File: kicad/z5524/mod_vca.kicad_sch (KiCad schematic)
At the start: 18 parts, among them U12 TL074, U13 AS3364

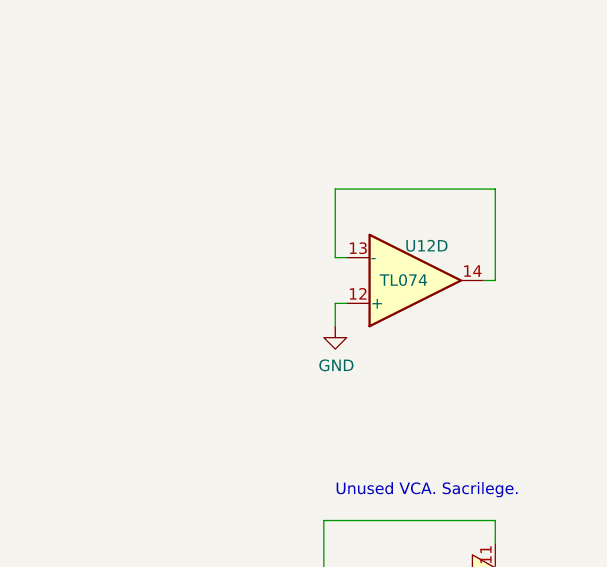
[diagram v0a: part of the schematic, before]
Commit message: move blocks into board for eval
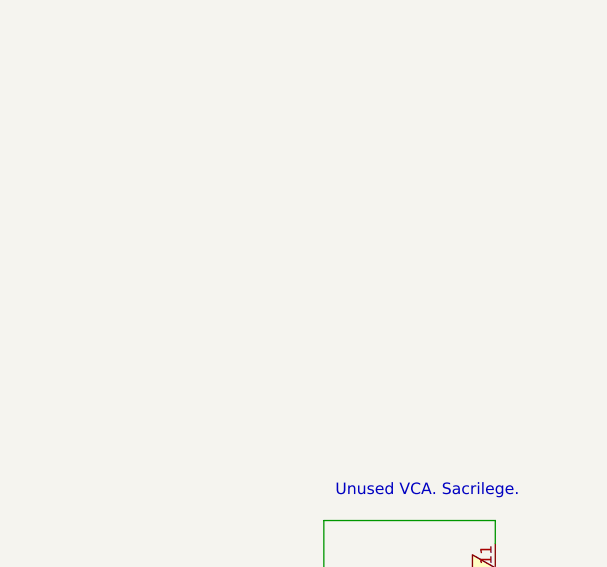
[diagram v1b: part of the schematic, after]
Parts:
- removed unit 4 of U12

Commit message: update to kicad 7
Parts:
- renumbered C39 to C15, C44 to C16, C67 to C18, C66 to C21, C41 to C42, C40 to C46, C42 to C51, C43 to C52, R54 to R19, R86 to R25, R81 to R26, R57 to R27, R85 to R29, R53 to R63, R87 to R64, R55 to R65, U13 to U6, U12 to U8
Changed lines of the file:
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@@
   (symbol (lib_id "Amplifier_Operational:TL074") (at 55.88 240.03 0) (unit 5)
     (in_bom yes) (on_board yes) (fields_autoplaced)
-    (property "Reference" "U12" (id 0) (at 53.975 239.1953 0)
+    (property "Reference" "U8" (id 0) (at 53.975 239.1953 0)
       (effects (font (size 1.27 1.27)) (justify left))
     )
@@
   (symbol (lib_name "AS3364_2") (lib_id "Audio:AS3364") (at 156.21 111.76 0) (unit 3)
     (in_bom yes) (on_board yes) (fields_autoplaced)
-    (property "Reference" "U13" (id 0) (at 160.02 116.84 0))
+    (property "Reference" "U6" (id 0) (at 160.02 116.84 0))
     (property "Value" "AS3364" (id 1) (at 162.56 114.3 0))
     (property "Footprint" "Package_SO:SOIC-16_3.9x9.9mm_P1.27mm" (id 2) (at 158.75 113.03 0)
@@
   (symbol (lib_id "Device:R") (at 180.34 54.61 270) (unit 1)
     (in_bom yes) (on_board yes)
-    (property "Reference" "R55" (id 0) (at 180.34 52.07 90))
+    (property "Reference" "R65" (id 0) (at 180.34 52.07 90))
     (property "Value" "47k" (id 1) (at 180.34 57.15 90))
     (property "Footprint" "Resistor_SMD:R_0603_1608Metric" (id 2) (at 180.34 52.832 90)
@@
   (symbol (lib_id "Amplifier_Operational:TL074") (at 180.34 69.85 0) (mirror x) (unit 3)
     (in_bom yes) (on_board yes)
-    (property "Reference" "U12" (id 0) (at 181.61 64.77 0))
+    (property "Reference" "U8" (id 0) (at 181.61 64.77 0))
     (property "Value" "TL074" (id 1) (at 180.34 69.85 0))
     (property "Footprint" "Package_SO:TSSOP-14_4.4x5mm_P0.65mm" (id 2) (at 179.07 72.39 0)
@@
   (symbol (lib_id "Device:C") (at 180.34 46.99 90) (unit 1)
     (in_bom yes) (on_board yes)
-    (property "Reference" "C43" (id 0) (at 178.435 42.545 0))
+    (property "Reference" "C52" (id 0) (at 178.435 42.545 0))
     (property "Value" "33p" (id 1) (at 182.245 42.545 0))
     (property "Footprint" "Capacitor_SMD:C_0603_1608Metric" (id 2) (at 184.15 46.0248 0)
@@
   (symbol (lib_id "Amplifier_Operational:TL074") (at 180.34 160.02 0) (mirror x) (unit 2)
     (in_bom yes) (on_board yes)
-    (property "Reference" "U12" (id 0) (at 181.61 154.94 0))
+    (property "Reference" "U8" (id 0) (at 181.61 154.94 0))
     (property "Value" "TL074" (id 1) (at 179.07 160.02 0))
     (property "Footprint" "Package_SO:TSSOP-14_4.4x5mm_P0.65mm" (id 2) (at 179.07 162.56 0)
@@
   (symbol (lib_id "Device:R") (at 143.51 67.31 90) (unit 1)
     (in_bom yes) (on_board yes)
-    (property "Reference" "R53" (id 0) (at 143.51 64.77 90))
+    (property "Reference" "R63" (id 0) (at 143.51 64.77 90))
     (property "Value" "47k" (id 1) (at 143.51 69.85 90))
     (property "Footprint" "Resistor_SMD:R_0603_1608Metric" (id 2) (at 143.51 69.088 90)
@@
   (symbol (lib_id "Audio:AS3364") (at 154.94 67.31 0) (unit 5)
     (in_bom yes) (on_board yes) (fields_autoplaced)
-    (property "Reference" "U13" (id 0) (at 158.75 72.39 0))
+    (property "Reference" "U6" (id 0) (at 158.75 72.39 0))
     (property "Value" "AS3364" (id 1) (at 161.29 69.85 0))
     (property "Footprint" "Package_SO:SOIC-16_3.9x9.9mm_P1.27mm" (id 2) (at 157.48 68.58 0)
@@
   (symbol (lib_id "Device:R") (at 374.65 213.36 270) (unit 1)
     (in_bom yes) (on_board yes)
-    (property "Reference" "R87" (id 0) (at 374.65 210.82 90))
+    (property "Reference" "R64" (id 0) (at 374.65 210.82 90))
     (property "Value" "47k" (id 1) (at 374.65 215.9 90))
     (property "Footprint" "Resistor_SMD:R_0603_1608Metric" (id 2) (at 374.65 211.582 90)
@@
   (symbol (lib_id "Device:R") (at 69.85 237.49 180) (unit 1)
     (in_bom yes) (on_board yes)
-    (property "Reference" "R81" (id 0) (at 66.04 234.95 0))
+    (property "Reference" "R26" (id 0) (at 66.04 234.95 0))
     (property "Value" "100" (id 1) (at 66.04 237.49 0))
     (property "Footprint" "Resistor_SMD:R_0603_1608Metric" (id 2) (at 71.628 237.49 90)
@@
   (symbol (lib_name "AS3364_1") (lib_id "Audio:AS3364") (at 156.21 157.48 0) (unit 2)
     (in_bom yes) (on_board yes) (fields_autoplaced)
-    (property "Reference" "U13" (id 0) (at 160.02 162.56 0))
+    (property "Reference" "U6" (id 0) (at 160.02 162.56 0))
     (property "Value" "AS3364" (id 1) (at 162.56 160.02 0))
     (property "Footprint" "Package_SO:SOIC-16_3.9x9.9mm_P1.27mm" (id 2) (at 158.75 158.75 0)
@@
   (symbol (lib_id "Device:C") (at 69.85 246.38 0) (unit 1)
     (in_bom yes) (on_board yes)
-    (property "Reference" "C66" (id 0) (at 66.04 243.84 0))
+    (property "Reference" "C21" (id 0) (at 66.04 243.84 0))
     (property "Value" "5n" (id 1) (at 66.04 246.38 0))
     (property "Footprint" "Capacitor_SMD:C_0603_1608Metric" (id 2) (at 70.8152 250.19 0)
@@
   (symbol (lib_id "Device:C") (at 48.26 251.46 270) (unit 1)
     (in_bom yes) (on_board yes)
-    (property "Reference" "C40" (id 0) (at 44.45 252.73 90))
+    (property "Reference" "C46" (id 0) (at 44.45 252.73 90))
     (property "Value" "0.1u" (id 1) (at 44.45 250.19 90))
     (property "Footprint" "Capacitor_SMD:C_0603_1608Metric" (id 2) (at 44.45 252.4252 0)
@@
   (symbol (lib_id "Device:C") (at 180.34 92.71 90) (unit 1)
     (in_bom yes) (on_board yes)
-    (property "Reference" "C44" (id 0) (at 178.435 88.265 0))
+    (property "Reference" "C16" (id 0) (at 178.435 88.265 0))
     (property "Value" "33p" (id 1) (at 182.245 88.265 0))
     (property "Footprint" "Capacitor_SMD:C_0603_1608Metric" (id 2) (at 184.15 91.7448 0)
@@
   (symbol (lib_name "AS3364_3") (lib_id "Audio:AS3364") (at 387.35 213.36 0) (unit 4)
     (in_bom yes) (on_board yes) (fields_autoplaced)
-    (property "Reference" "U13" (id 0) (at 391.16 218.44 0))
+    (property "Reference" "U6" (id 0) (at 391.16 218.44 0))
     (property "Value" "AS3364" (id 1) (at 393.7 215.9 0))
     (property "Footprint" "Package_SO:SOIC-16_3.9x9.9mm_P1.27mm" (id 2) (at 389.89 214.63 0)
@@
   (symbol (lib_id "Device:R") (at 144.78 157.48 90) (unit 1)
     (in_bom yes) (on_board yes)
-    (property "Reference" "R85" (id 0) (at 144.78 154.94 90))
+    (property "Reference" "R29" (id 0) (at 144.78 154.94 90))
     (property "Value" "47k" (id 1) (at 144.78 160.02 90))
     (property "Footprint" "Resistor_SMD:R_0603_1608Metric" (id 2) (at 144.78 159.258 90)
@@
   (symbol (lib_id "Device:C") (at 48.26 228.6 270) (unit 1)
     (in_bom yes) (on_board yes)
-    (property "Reference" "C39" (id 0) (at 44.45 229.87 90))
+    (property "Reference" "C15" (id 0) (at 44.45 229.87 90))
     (property "Value" "0.1u" (id 1) (at 44.45 227.33 90))
     (property "Footprint" "Capacitor_SMD:C_0603_1608Metric" (id 2) (at 44.45 229.5652 0)
@@
   (symbol (lib_id "Device:R") (at 180.34 100.33 270) (unit 1)
     (in_bom yes) (on_board yes)
-    (property "Reference" "R57" (id 0) (at 180.34 97.79 90))
+    (property "Reference" "R27" (id 0) (at 180.34 97.79 90))
     (property "Value" "47k" (id 1) (at 180.34 102.87 90))
     (property "Footprint" "Resistor_SMD:R_0603_1608Metric" (id 2) (at 180.34 98.552 90)
@@
   (symbol (lib_id "Device:R") (at 180.34 146.05 270) (unit 1)
     (in_bom yes) (on_board yes)
-    (property "Reference" "R86" (id 0) (at 180.34 143.51 90))
+    (property "Reference" "R25" (id 0) (at 180.34 143.51 90))
     (property "Value" "47k" (id 1) (at 180.34 148.59 90))
     (property "Footprint" "Resistor_SMD:R_0603_1608Metric" (id 2) (at 180.34 144.272 90)
@@
   (symbol (lib_id "Device:R") (at 143.51 111.76 90) (unit 1)
     (in_bom yes) (on_board yes)
-    (property "Reference" "R54" (id 0) (at 143.51 109.22 90))
+    (property "Reference" "R19" (id 0) (at 143.51 109.22 90))
     (property "Value" "47k" (id 1) (at 143.51 114.3 90))
     (property "Footprint" "Resistor_SMD:R_0603_1608Metric" (id 2) (at 143.51 113.538 90)
@@
   (symbol (lib_id "Amplifier_Operational:TL074") (at 180.34 114.3 0) (mirror x) (unit 1)
     (in_bom yes) (on_board yes)
-    (property "Reference" "U12" (id 0) (at 181.61 110.49 0))
+    (property "Reference" "U8" (id 0) (at 181.61 110.49 0))
     (property "Value" "TL074" (id 1) (at 179.07 114.3 0))
     (property "Footprint" "Package_SO:TSSOP-14_4.4x5mm_P0.65mm" (id 2) (at 179.07 116.84 0)
@@
   (symbol (lib_name "AS3364_4") (lib_id "Audio:AS3364") (at 82.55 234.95 0) (unit 1)
     (in_bom yes) (on_board yes)
-    (property "Reference" "U13" (id 0) (at 91.44 237.49 0))
+    (property "Reference" "U6" (id 0) (at 91.44 237.49 0))
     (property "Value" "AS3364" (id 1) (at 92.71 233.68 0))
     (property "Footprint" "Package_SO:SOIC-16_3.9x9.9mm_P1.27mm" (id 2) (at 85.09 236.22 0)
@@
   (symbol (lib_id "Device:C") (at 180.34 138.43 90) (unit 1)
     (in_bom yes) (on_board yes)
-    (property "Reference" "C67" (id 0) (at 178.435 133.985 0))
+    (property "Reference" "C18" (id 0) (at 178.435 133.985 0))
     (property "Value" "33p" (id 1) (at 182.245 133.985 0))
     (property "Footprint" "Capacitor_SMD:C_0603_1608Metric" (id 2) (at 184.15 137.4648 0)
@@
   (symbol (lib_id "Device:C") (at 78.74 224.79 270) (unit 1)
     (in_bom yes) (on_board yes)
-    (property "Reference" "C41" (id 0) (at 74.93 226.06 90))
+    (property "Reference" "C42" (id 0) (at 74.93 226.06 90))
     (property "Value" "0.1u" (id 1) (at 74.93 223.52 90))
     (property "Footprint" "Capacitor_SMD:C_0603_1608Metric" (id 2) (at 74.93 225.7552 0)
@@
   (symbol (lib_id "Device:C") (at 81.28 250.19 270) (unit 1)
     (in_bom yes) (on_board yes)
-    (property "Reference" "C42" (id 0) (at 82.55 254 90))
+    (property "Reference" "C51" (id 0) (at 82.55 254 90))
     (property "Value" "0.1u" (id 1) (at 82.55 246.38 90))
     (property "Footprint" "Capacitor_SMD:C_0603_1608Metric" (id 2) (at 77.47 251.1552 0)

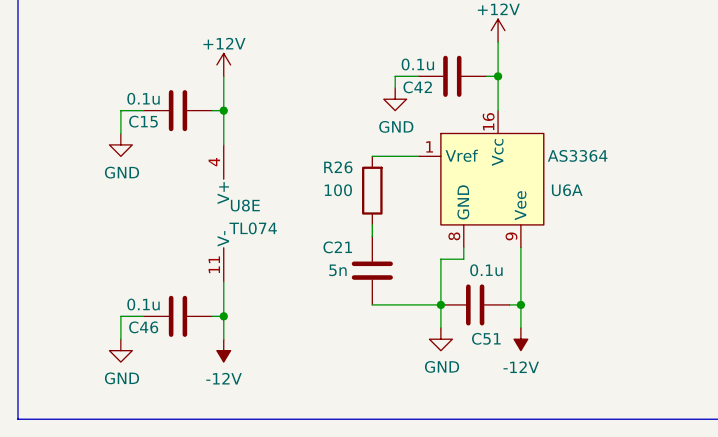
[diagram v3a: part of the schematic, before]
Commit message: update LCSC Part numbers, some modification to account for parts
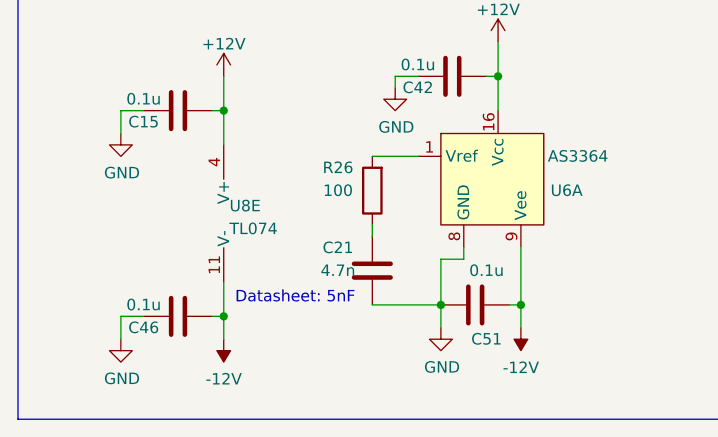
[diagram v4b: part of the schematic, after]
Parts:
- C21: value 5n -> 4.7n; LCSC Part (none) -> C53987
- R26: LCSC Part (none) -> C22775
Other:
- note added: "Datasheet: 5nF"
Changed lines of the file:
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@@
+    (effects (font (size 1.27 1.27)) (justify left bottom))
+  )
+  (text "Datasheet: 5nF" (at 54.61 250.19 0)
     (effects (font (size 1.27 1.27)) (justify left bottom))
   )
@@
       (effects (font (size 1.27 1.27)) hide)
     )
-    (property "LCSC Part" "" (at 69.85 237.49 0)
+    (property "LCSC Part" "C22775" (at 69.85 237.49 0)
       (effects (font (size 1.27 1.27)) hide)
     )
@@
       (effects (font (size 1.27 1.27)))
     )
-    (property "Value" "5n" (at 66.04 246.38 0)
+    (property "Value" "4.7n" (at 66.04 246.38 0)
       (effects (font (size 1.27 1.27)))
     )
@@
       (effects (font (size 1.27 1.27)) hide)
     )
-    (property "LCSC Part" "" (at 69.85 246.38 0)
-      (effects (font (size 1.27 1.27)) hide)
-    )
+    (property "LCSC Part" "C53987" (at 69.85 246.38 0)
+      (effects (font (size 1.27 1.27)) hide)
+    )

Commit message: fix symbol library
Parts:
- U6: symbol Audio:AS3364 -> z5524:AS3364
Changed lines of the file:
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@@
     )
   )
-  (symbol (lib_name "AS3364_2") (lib_id "Audio:AS3364") (at 156.21 111.76 0) (unit 3)
+  (symbol (lib_id "z5524:AS3364") (at 156.21 111.76 0) (unit 3)
     (in_bom yes) (on_board yes) (dnp no) (fields_autoplaced)
     (property "Reference" "U6" (at 160.02 116.84 0)
@@
     )
   )
-  (symbol (lib_id "Audio:AS3364") (at 154.94 67.31 0) (unit 5)
+  (symbol (lib_id "z5524:AS3364") (at 154.94 67.31 0) (unit 5)
     (in_bom yes) (on_board yes) (dnp no) (fields_autoplaced)
     (property "Reference" "U6" (at 158.75 72.39 0)
@@
     )
   )
-  (symbol (lib_name "AS3364_1") (lib_id "Audio:AS3364") (at 156.21 157.48 0) (unit 2)
+  (symbol (lib_id "z5524:AS3364") (at 156.21 157.48 0) (unit 2)
     (in_bom yes) (on_board yes) (dnp no) (fields_autoplaced)
     (property "Reference" "U6" (at 160.02 162.56 0)
@@
     )
   )
-  (symbol (lib_name "AS3364_3") (lib_id "Audio:AS3364") (at 387.35 213.36 0) (unit 4)
+  (symbol (lib_id "z5524:AS3364") (at 387.35 213.36 0) (unit 4)
     (in_bom yes) (on_board yes) (dnp no) (fields_autoplaced)
     (property "Reference" "U6" (at 391.16 218.44 0)
@@
     )
   )
-  (symbol (lib_name "AS3364_4") (lib_id "Audio:AS3364") (at 82.55 234.95 0) (unit 1)
+  (symbol (lib_id "z5524:AS3364") (at 82.55 234.95 0) (unit 1)
     (in_bom yes) (on_board yes) (dnp no)
     (property "Reference" "U6" (at 91.44 237.49 0)

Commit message: inc volt ref caps
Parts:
- C15, C42, C46, C51: LCSC (none) -> C14663; LCSC Part C14663 -> (none)
- C16, C18, C52: LCSC (none) -> C1663; LCSC Part C1663 -> (none)
- C21: LCSC (none) -> C53987; LCSC Part C53987 -> (none)
- R19, R25, R27, R29, R63, R64, R65: LCSC (none) -> C25819; LCSC Part C25819 -> (none)
- R26: LCSC (none) -> C22775; LCSC Part C22775 -> (none)
- U8: LCSC (none) -> C96507; LCSC Part C96507 -> (none)
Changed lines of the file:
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@@
       (effects (font (size 1.27 1.27)) hide)
     )
-    (property "LCSC Part" "C96507" (at 180.34 69.85 0)
+    (property "LCSC" "C96507" (at 180.34 69.85 0)
       (effects (font (size 1.27 1.27)) hide)
     )
@@
       (effects (font (size 1.27 1.27)) hide)
     )
-    (property "LCSC Part" "C25819" (at 180.34 54.61 0)
+    (property "LCSC" "C25819" (at 180.34 54.61 0)
       (effects (font (size 1.27 1.27)) hide)
     )
@@
       (effects (font (size 1.27 1.27)) hide)
     )
-    (property "LCSC Part" "C96507" (at 180.34 69.85 0)
+    (property "LCSC" "C96507" (at 180.34 69.85 0)
       (effects (font (size 1.27 1.27)) hide)
     )
@@
       (effects (font (size 1.27 1.27)) hide)
     )
-    (property "LCSC Part" "C1663" (at 180.34 46.99 0)
+    (property "LCSC" "C1663" (at 180.34 46.99 0)
       (effects (font (size 1.27 1.27)) hide)
     )
@@
       (effects (font (size 1.27 1.27)) hide)
     )
-    (property "LCSC Part" "C96507" (at 180.34 69.85 0)
+    (property "LCSC" "C96507" (at 180.34 69.85 0)
       (effects (font (size 1.27 1.27)) hide)
     )
@@
       (effects (font (size 1.27 1.27)) hide)
     )
-    (property "LCSC Part" "C25819" (at 143.51 67.31 0)
+    (property "LCSC" "C25819" (at 143.51 67.31 0)
       (effects (font (size 1.27 1.27)) hide)
     )
@@
       (effects (font (size 1.27 1.27)) hide)
     )
-    (property "LCSC Part" "C25819" (at 374.65 213.36 0)
+    (property "LCSC" "C25819" (at 374.65 213.36 0)
       (effects (font (size 1.27 1.27)) hide)
     )
@@
       (effects (font (size 1.27 1.27)) hide)
     )
-    (property "LCSC Part" "C22775" (at 69.85 237.49 0)
+    (property "LCSC" "C22775" (at 69.85 237.49 0)
       (effects (font (size 1.27 1.27)) hide)
     )
@@
       (effects (font (size 1.27 1.27)) hide)
     )
-    (property "LCSC Part" "C53987" (at 69.85 246.38 0)
+    (property "LCSC" "C53987" (at 69.85 246.38 0)
       (effects (font (size 1.27 1.27)) hide)
     )
@@
       (effects (font (size 1.27 1.27)) hide)
     )
-    (property "LCSC Part" "C14663" (at 48.26 251.46 0)
+    (property "LCSC" "C14663" (at 48.26 251.46 0)
       (effects (font (size 1.27 1.27)) hide)
     )
@@
       (effects (font (size 1.27 1.27)) hide)
     )
-    (property "LCSC Part" "C1663" (at 180.34 92.71 0)
+    (property "LCSC" "C1663" (at 180.34 92.71 0)
       (effects (font (size 1.27 1.27)) hide)
     )
@@
       (effects (font (size 1.27 1.27)) hide)
     )
-    (property "LCSC Part" "C25819" (at 144.78 157.48 0)
+    (property "LCSC" "C25819" (at 144.78 157.48 0)
       (effects (font (size 1.27 1.27)) hide)
     )
@@
       (effects (font (size 1.27 1.27)) hide)
     )
-    (property "LCSC Part" "C14663" (at 48.26 228.6 0)
+    (property "LCSC" "C14663" (at 48.26 228.6 0)
       (effects (font (size 1.27 1.27)) hide)
     )
@@
       (effects (font (size 1.27 1.27)) hide)
     )
-    (property "LCSC Part" "C25819" (at 180.34 100.33 0)
+    (property "LCSC" "C25819" (at 180.34 100.33 0)
       (effects (font (size 1.27 1.27)) hide)
     )
@@
       (effects (font (size 1.27 1.27)) hide)
     )
-    (property "LCSC Part" "C25819" (at 180.34 146.05 0)
+    (property "LCSC" "C25819" (at 180.34 146.05 0)
       (effects (font (size 1.27 1.27)) hide)
     )
@@
       (effects (font (size 1.27 1.27)) hide)
     )
-    (property "LCSC Part" "C25819" (at 143.51 111.76 0)
+    (property "LCSC" "C25819" (at 143.51 111.76 0)
       (effects (font (size 1.27 1.27)) hide)
     )
@@
       (effects (font (size 1.27 1.27)) hide)
     )
-    (property "LCSC Part" "C96507" (at 180.34 69.85 0)
+    (property "LCSC" "C96507" (at 180.34 69.85 0)
       (effects (font (size 1.27 1.27)) hide)
     )
@@
       (effects (font (size 1.27 1.27)) hide)
     )
-    (property "LCSC Part" "C1663" (at 180.34 138.43 0)
+    (property "LCSC" "C1663" (at 180.34 138.43 0)
       (effects (font (size 1.27 1.27)) hide)
     )
@@
       (effects (font (size 1.27 1.27)) hide)
     )
-    (property "LCSC Part" "C14663" (at 78.74 224.79 0)
+    (property "LCSC" "C14663" (at 78.74 224.79 0)
       (effects (font (size 1.27 1.27)) hide)
     )
@@
       (effects (font (size 1.27 1.27)) hide)
     )
-    (property "LCSC Part" "C14663" (at 81.28 250.19 0)
-      (effects (font (size 1.27 1.27)) hide)
-    )
+    (property "LCSC" "C14663" (at 81.28 250.19 0)
+      (effects (font (size 1.27 1.27)) hide)
+    )
